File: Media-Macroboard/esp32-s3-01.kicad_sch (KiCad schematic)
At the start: 25 parts, among them Q1 MMBT3904LT3G, Q2 MMBT3904LT3G, U1 ESP32-S3-WROOM-1, U2 USBLC6-2SC6, U3 CP2102N-Axx-xQFN20

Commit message: First productable version
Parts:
- C9: footprint Capacitor_SMD:C_0805_2012Metric_Pad1.18x1.45mm_HandSolder -> Capacitor_SMD:C_1206_3216Metric
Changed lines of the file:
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@@
 			)
 		)
-		(property "Footprint" "Capacitor_SMD:C_0805_2012Metric_Pad1.18x1.45mm_HandSolder"
+		(property "Footprint" "Capacitor_SMD:C_1206_3216Metric"
 			(at 69.85 32.7152 0)
 			(effects

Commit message: Update
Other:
- note added: "Microprocessor"
- moved on the sheet: C10, C11, U1

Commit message: Made four-layer version
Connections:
- net LED1: no longer U1.21 (IO13)
- net LED2: no longer U1.22 (IO14)
- net LED3: no longer U1.8 (IO15)
- net LED4: no longer U1.9 (IO16)
- net Light: no longer U1.39 (IO1)
- no-connect marks 22 -> 27
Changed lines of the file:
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@@
+	)
+	(no_connect
+		(at 214.63 72.39)
 	)
 	(no_connect
@@
 	)
 	(no_connect
+		(at 214.63 105.41)
+	)
+	(no_connect
 		(at 245.11 107.95)
 	)
 	(no_connect
+		(at 214.63 110.49)
+	)
+	(no_connect
 		(at 220.98 144.78)
 	)
@@
 	)
 	(no_connect
+		(at 214.63 107.95)
+	)
+	(no_connect
 		(at 200.66 147.32)
+	)
+	(no_connect
+		(at 214.63 102.87)
 	)
 	(wire
@@
 		)
 	)
-	(label "LED3"
-		(at 214.63 107.95 180)
-		(effects
-			(font
-				(size 1.27 1.27)
-			)
-			(justify right bottom)
-		)
-	)
 	(label "ROW_3"
 		(at 214.63 100.33 180)
@@
 		)
 	)
-	(label "Light"
-		(at 214.63 72.39 180)
-		(effects
-			(font
-				(size 1.27 1.27)
-			)
-			(justify right bottom)
-		)
-	)
 	(label "CHIP_PU"
 		(at 80.01 151.13 0)
@@
 		)
 	)
-	(label "LED1"
-		(at 214.63 102.87 180)
-		(effects
-			(font
-				(size 1.27 1.27)
-			)
-			(justify right bottom)
-		)
-	)
 	(label "COL_3"
 		(at 138.43 137.16 180)
@@
 		)
 	)
-	(label "LED4"
-		(at 214.63 110.49 180)
-		(effects
-			(font
-				(size 1.27 1.27)
-			)
-			(justify right bottom)
-		)
-	)
 	(label "COL_2"
 		(at 138.43 134.62 180)
 		(effects
 			(font
-				(size 1.27 1.27)
-			)
-			(justify right bottom)
-		)
-	)
-	(label "LED2"
-		(at 214.63 105.41 180)
-		(effects
-			(font

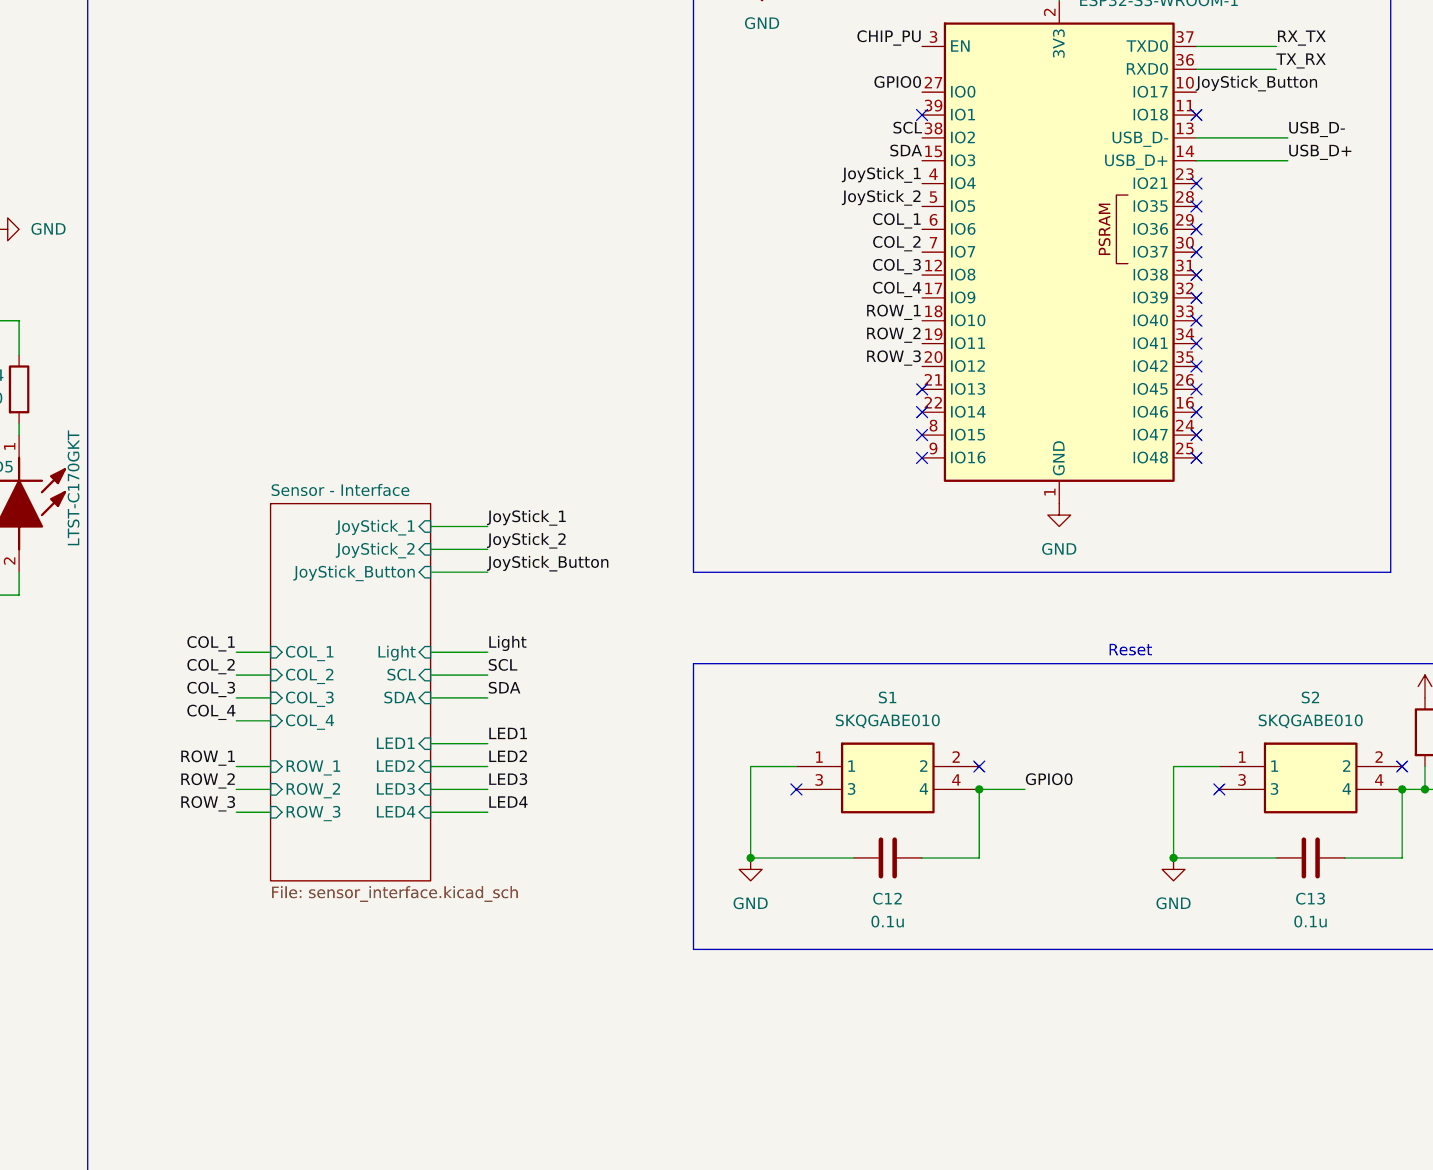
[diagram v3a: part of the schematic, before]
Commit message: Added more rows and columns
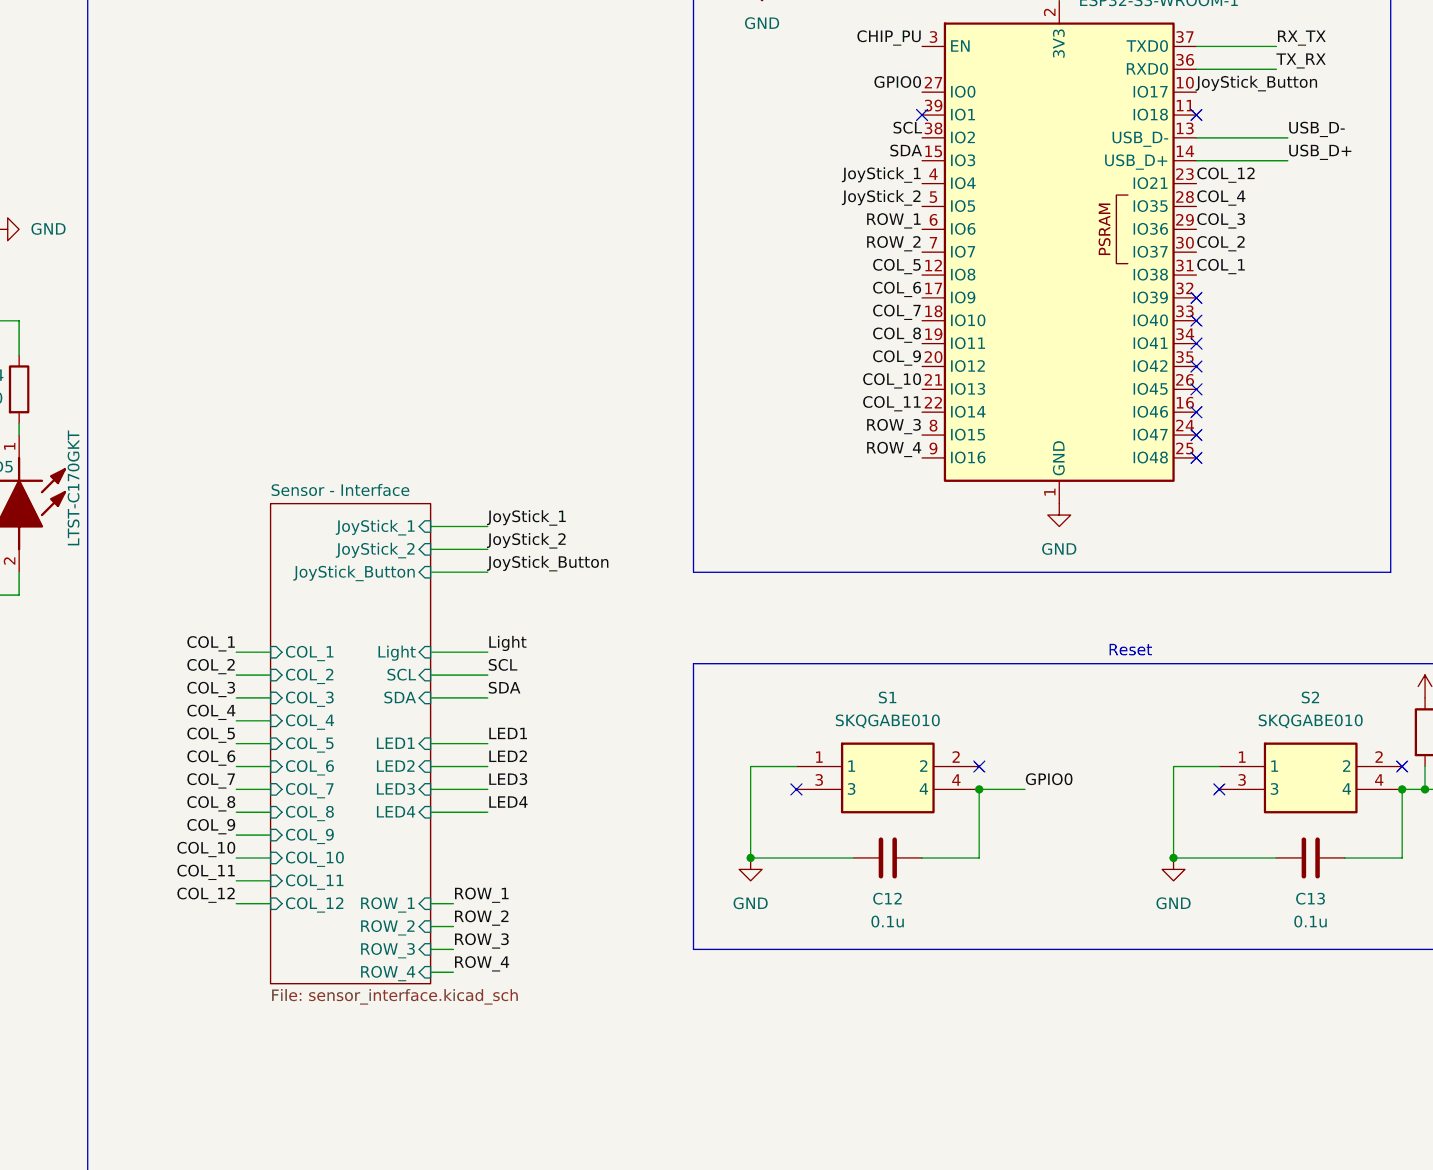
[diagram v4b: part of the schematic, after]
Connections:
- net COL_1: now also U1.31 (IO38); no longer U1.6 (IO6)
- net COL_2: now also U1.30 (IO37); no longer U1.7 (IO7)
- net COL_3: now also U1.29 (IO36); no longer U1.12 (IO8)
- net COL_4: now also U1.28 (IO35); no longer U1.17 (IO9)
- net ROW_1: now also U1.6 (IO6); no longer U1.18 (IO10)
- net ROW_2: now also U1.7 (IO7); no longer U1.19 (IO11)
- net ROW_3: now also U1.8 (IO15); no longer U1.20 (IO12)
- net COL_10: now reaches U1.21 (IO13)
- net COL_11: now reaches U1.22 (IO14)
- net COL_12: now reaches U1.23 (IO21)
- net ROW_4: now reaches U1.9 (IO16)
- new net COL_5: U1.12 (IO8)
- new net COL_6: U1.17 (IO9)
- new net COL_7: U1.18 (IO10)
- new net COL_8: U1.19 (IO11)
- new net COL_9: U1.20 (IO12)
- no-connect marks 27 -> 18
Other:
- sheet Sensor - Interface ports: added COL_10, COL_11, COL_12, COL_5, COL_6, COL_7, COL_8, COL_9, ROW_4; removed none
